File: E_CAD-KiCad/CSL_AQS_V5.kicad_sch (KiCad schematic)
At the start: 10 parts, among them J2 Grove STEMMA, J3 Grove STEMMA

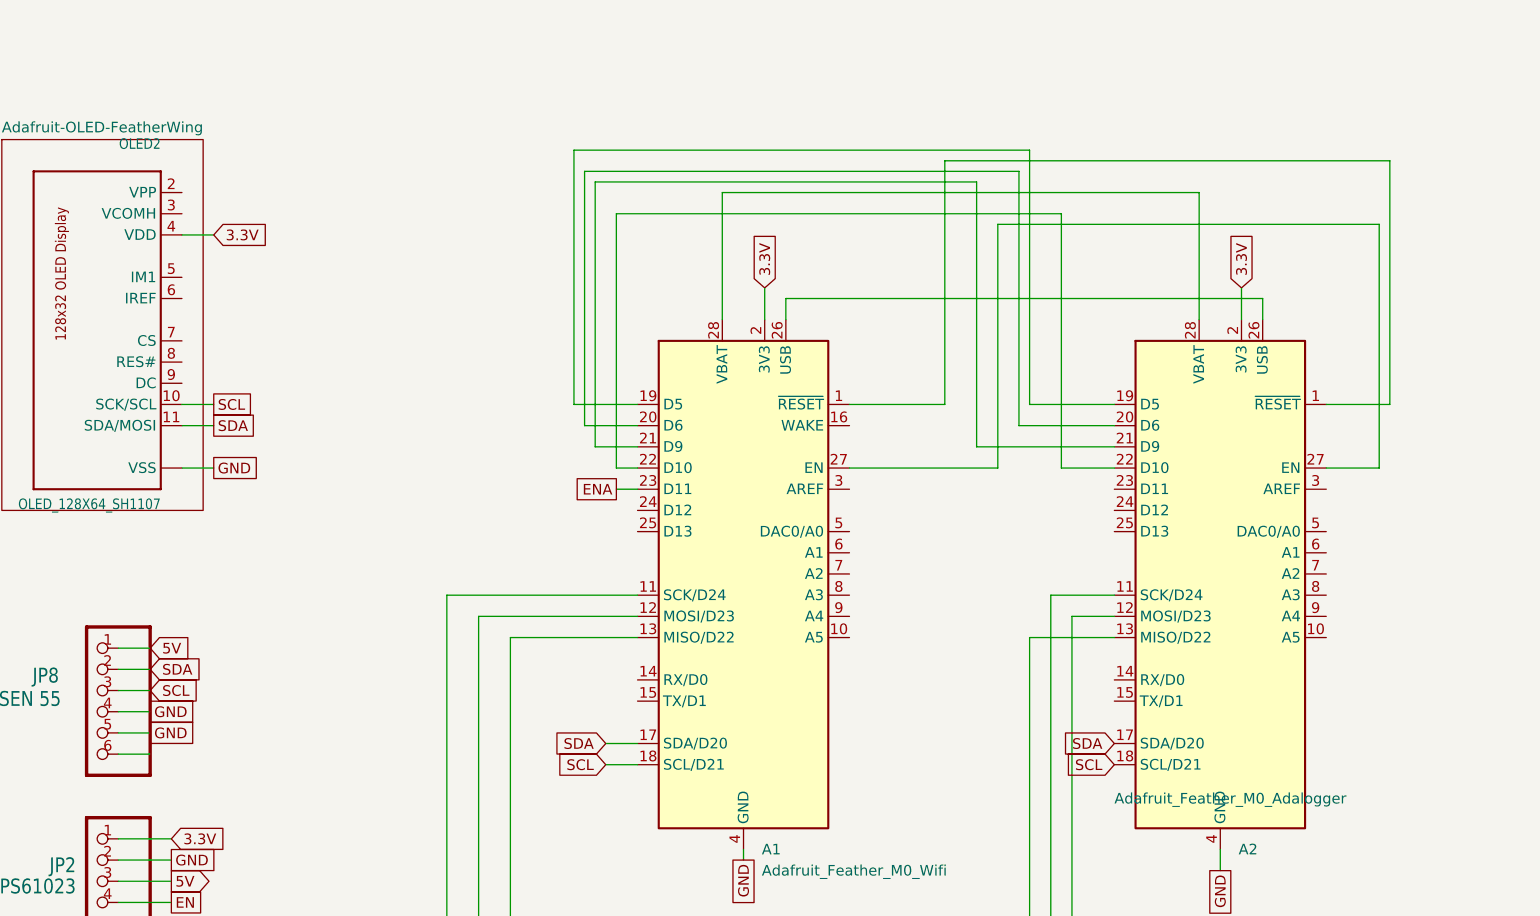
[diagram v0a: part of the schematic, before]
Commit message: Reorganized E-CAD to updated version (5)
Updated to most recent version, version 5
Made updates to the schematic and PCB board in relation to SEN55
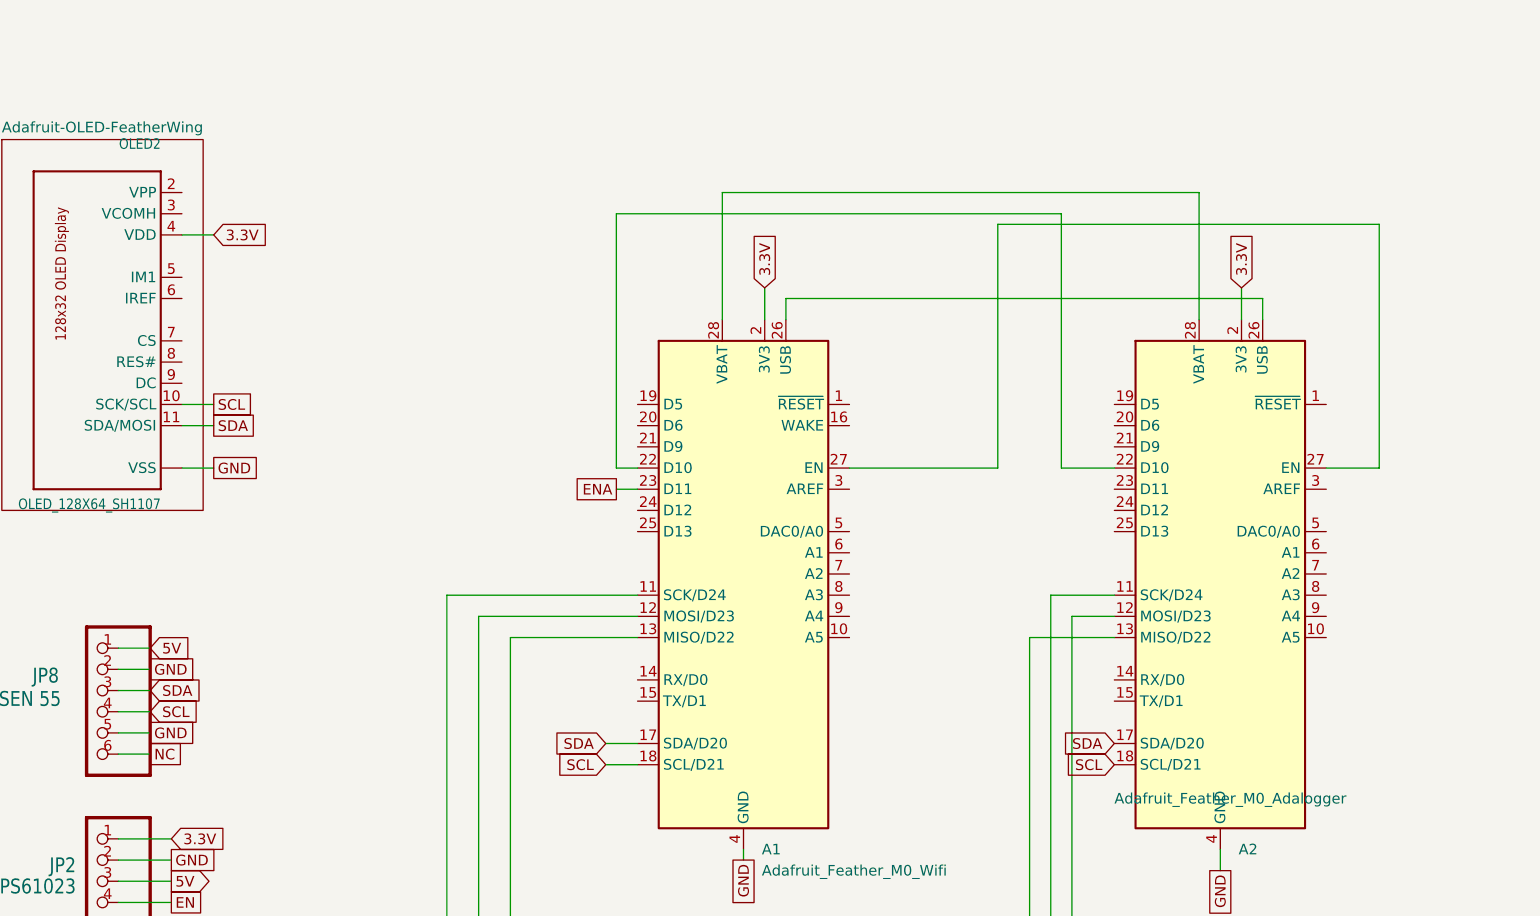
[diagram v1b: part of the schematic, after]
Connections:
- net GND: now also JP8.2; no longer JP8.4
- net NC: now also JP8.6
- net SCL: now also JP8.4; no longer JP8.3
- net SDA: now also JP8.3; no longer JP8.2
- net at A1.1 (~{RESET}): no longer A2.1 (~{RESET})
- net at A1.19 (D5): no longer A2.19 (D5)
- net at A1.20 (D6): no longer A2.20 (D6)
- net at A1.21 (D9): no longer A2.21 (D9)
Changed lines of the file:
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@@
 	(wire
 		(pts
-			(xy 139.7 69.85) (xy 149.86 69.85)
-		)
-		(stroke
-			(width 0)
-			(type default)
-		)
-	)
-	(wire
-		(pts
-			(xy 133.35 43.18) (xy 133.35 74.93)
+			(xy 30.48 104.14) (xy 34.29 104.14)
 		)
 		(stroke
@@
 	(wire
 		(pts
-			(xy 182.88 40.64) (xy 182.88 69.85)
-		)
-		(stroke
-			(width 0)
-			(type default)
-		)
-	)
-	(wire
-		(pts
 			(xy 91.44 175.26) (xy 93.98 175.26)
 		)
@@
 	(wire
 		(pts
-			(xy 129.54 40.64) (xy 182.88 40.64)
-		)
-		(stroke
-			(width 0)
-			(type default)
-		)
-	)
-	(wire
-		(pts
 			(xy 30.48 148.59) (xy 35.56 148.59)
 		)
@@
 	(wire
 		(pts
-			(xy 87.63 43.18) (xy 133.35 43.18)
-		)
-		(stroke
-			(width 0)
-			(type default)
-		)
-	)
-	(wire
-		(pts
-			(xy 129.54 69.85) (xy 129.54 40.64)
-		)
-		(stroke
-			(width 0)
-			(type default)
-		)
-	)
-	(wire
-		(pts
 			(xy 30.48 124.46) (xy 36.83 124.46)
 		)
@@
 	(wire
 		(pts
-			(xy 138.43 72.39) (xy 149.86 72.39)
-		)
-		(stroke
-			(width 0)
-			(type default)
-		)
-	)
-	(wire
-		(pts
 			(xy 30.48 151.13) (xy 35.56 151.13)
 		)
@@
 	(wire
 		(pts
-			(xy 85.09 69.85) (xy 85.09 39.37)
-		)
-		(stroke
-			(width 0)
-			(type default)
-		)
-	)
-	(wire
-		(pts
 			(xy 160.02 59.69) (xy 160.02 44.45)
 		)
@@
 	(wire
 		(pts
+			(xy 30.48 101.6) (xy 34.29 101.6)
+		)
+		(stroke
+			(width 0)
+			(type default)
+		)
+	)
+	(wire
+		(pts
 			(xy 30.48 153.67) (xy 35.56 153.67)
 		)
@@
 	(wire
 		(pts
+			(xy 30.48 106.68) (xy 34.29 106.68)
+		)
+		(stroke
+			(width 0)
+			(type default)
+		)
+	)
+	(wire
+		(pts
 			(xy 139.7 97.79) (xy 149.86 97.79)
 		)
@@
 	(wire
 		(pts
-			(xy 118.11 69.85) (xy 129.54 69.85)
-		)
-		(stroke
-			(width 0)
-			(type default)
-		)
-	)
-	(wire
-		(pts
-			(xy 182.88 69.85) (xy 175.26 69.85)
-		)
-		(stroke
-			(width 0)
-			(type default)
-		)
-	)
-	(wire
-		(pts
 			(xy 88.9 113.03) (xy 92.71 113.03)
 		)
@@
 	(wire
 		(pts
-			(xy 87.63 74.93) (xy 87.63 43.18)
-		)
-		(stroke
-			(width 0)
-			(type default)
-		)
-	)
-	(wire
-		(pts
 			(xy 165.1 55.88) (xy 165.1 59.69)
 		)
@@
 	(wire
 		(pts
-			(xy 139.7 39.37) (xy 139.7 69.85)
-		)
-		(stroke
-			(width 0)
-			(type default)
-		)
-	)
-	(wire
-		(pts
 			(xy 91.44 177.8) (xy 93.98 177.8)
 		)
@@
 	(wire
 		(pts
-			(xy 30.48 101.6) (xy 34.29 101.6)
-		)
-		(stroke
-			(width 0)
-			(type default)
-		)
-	)
-	(wire
-		(pts
 			(xy 92.71 92.71) (xy 69.85 92.71)
 		)
@@
 	(wire
 		(pts
-			(xy 138.43 41.91) (xy 138.43 72.39)
-		)
-		(stroke
-			(width 0)
-			(type default)
-		)
-	)
-	(wire
-		(pts
 			(xy 135.89 48.26) (xy 181.61 48.26)
 		)
@@
 	(wire
 		(pts
-			(xy 86.36 72.39) (xy 86.36 41.91)
-		)
-		(stroke
-			(width 0)
-			(type default)
-		)
-	)
-	(wire
-		(pts
-			(xy 92.71 74.93) (xy 87.63 74.93)
-		)
-		(stroke
-			(width 0)
-			(type default)
-		)
-	)
-	(wire
-		(pts
 			(xy 30.48 121.92) (xy 36.83 121.92)
 		)
@@
 	(wire
 		(pts
-			(xy 133.35 74.93) (xy 149.86 74.93)
-		)
-		(stroke
-			(width 0)
-			(type default)
-		)
-	)
-	(wire
-		(pts
 			(xy 73.66 137.16) (xy 144.78 137.16)
 		)
@@
 	(wire
 		(pts
-			(xy 85.09 39.37) (xy 139.7 39.37)
-		)
-		(stroke
-			(width 0)
-			(type default)
-		)
-	)
-	(wire
-		(pts
 			(xy 167.64 59.69) (xy 167.64 57.15)
 		)
@@
 	(wire
 		(pts
-			(xy 92.71 72.39) (xy 86.36 72.39)
-		)
-		(stroke
-			(width 0)
-			(type default)
-		)
-	)
-	(wire
-		(pts
 			(xy 38.1 77.47) (xy 41.91 77.47)
 		)
@@
 	(wire
 		(pts
-			(xy 30.48 104.14) (xy 34.29 104.14)
-		)
-		(stroke
-			(width 0)
-			(type default)
-		)
-	)
-	(wire
-		(pts
 			(xy 60.96 165.1) (xy 64.77 165.1)
 		)
@@
 	(wire
 		(pts
-			(xy 30.48 106.68) (xy 34.29 106.68)
-		)
-		(stroke
-			(width 0)
-			(type default)
-		)
-	)
-	(wire
-		(pts
 			(xy 77.47 134.62) (xy 139.7 134.62)
 		)
@@
 	(wire
 		(pts
-			(xy 92.71 69.85) (xy 85.09 69.85)
-		)
-		(stroke
-			(width 0)
-			(type default)
-		)
-	)
-	(wire
-		(pts
 			(xy 92.71 95.25) (xy 73.66 95.25)
 		)
@@
 		(pts
 			(xy 90.17 77.47) (xy 90.17 46.99)
-		)
-		(stroke
-			(width 0)
-			(type default)
-		)
-	)
-	(wire
-		(pts
-			(xy 86.36 41.91) (xy 138.43 41.91)
 		)
 		(stroke
@@
 	(global_label "GND"
 		(shape passive)
-		(at 34.29 106.68 0)
-		(fields_autoplaced yes)
-		(effects
-			(font
-				(size 1.27 1.27)
-			)
-			(justify left)
-		)
-		(property "Intersheetrefs" "${INTERSHEET_REFS}"
-			(at 40.0344 106.68 0)
+		(at 34.29 101.6 0)
+		(fields_autoplaced yes)
+		(effects
+			(font
+				(size 1.27 1.27)
+			)
+			(justify left)
+		)
+		(property "Intersheetrefs" "${INTERSHEET_REFS}"
+			(at 40.0344 101.6 0)
 			(effects
 				(font
@@
 	(global_label "SDA"
 		(shape input)
-		(at 34.29 101.6 0)
-		(fields_autoplaced yes)
-		(effects
-			(font
-				(size 1.27 1.27)
-			)
-			(justify left)
-		)
-		(property "Intersheetrefs" "${INTERSHEET_REFS}"
-			(at 40.8433 101.6 0)
+		(at 34.29 104.14 0)
+		(fields_autoplaced yes)
+		(effects
+			(font
+				(size 1.27 1.27)
+			)
+			(justify left)
+		)
+		(property "Intersheetrefs" "${INTERSHEET_REFS}"
+			(at 40.8433 104.14 0)
 			(effects
 				(font
@@
 	(global_label "SCL"
 		(shape input)
-		(at 34.29 104.14 0)
-		(fields_autoplaced yes)
-		(effects
-			(font
-				(size 1.27 1.27)
-			)
-			(justify left)
-		)
-		(property "Intersheetrefs" "${INTERSHEET_REFS}"
-			(at 40.7828 104.14 0)
+		(at 34.29 106.68 0)
+		(fields_autoplaced yes)
+		(effects
+			(font
+				(size 1.27 1.27)
+			)
+			(justify left)
+		)
+		(property "Intersheetrefs" "${INTERSHEET_REFS}"
+			(at 40.7828 106.68 0)
 			(effects
 				(font
@@
 		(property "Intersheetrefs" "${INTERSHEET_REFS}"
 			(at 40.0344 148.59 0)
+			(effects
+				(font
+					(size 1.27 1.27)
+				)
+				(justify left)
+				(hide yes)
+			)
+		)
+	)
+	(global_label "NC"
+		(shape passive)
+		(at 34.29 111.76 0)
+		(fields_autoplaced yes)
+		(effects
+			(font
+				(size 1.27 1.27)
+			)
+			(justify left)
+		)
+		(property "Intersheetrefs" "${INTERSHEET_REFS}"
+			(at 38.7644 111.76 0)
 			(effects
 				(font
@@
 		)
 		(instances
-			(project "CSL_AQS_V1"
+			(project "CSL_AQS_V5"
 				(path "/0298e1a2-41ac-46e9-9543-4e7b3ae3dfa6"
 					(page "4")
@@
 		)
 		(instances
-			(project "CSL_AQS_V1"
+			(project "CSL_AQS_V5"
 				(path "/0298e1a2-41ac-46e9-9543-4e7b3ae3dfa6"
 					(page "3")
@@
 		)
 		(instances
-			(project "CSL_AQS_V1"
+			(project "CSL_AQS_V5"
 				(path "/0298e1a2-41ac-46e9-9543-4e7b3ae3dfa6"
 					(page "2")

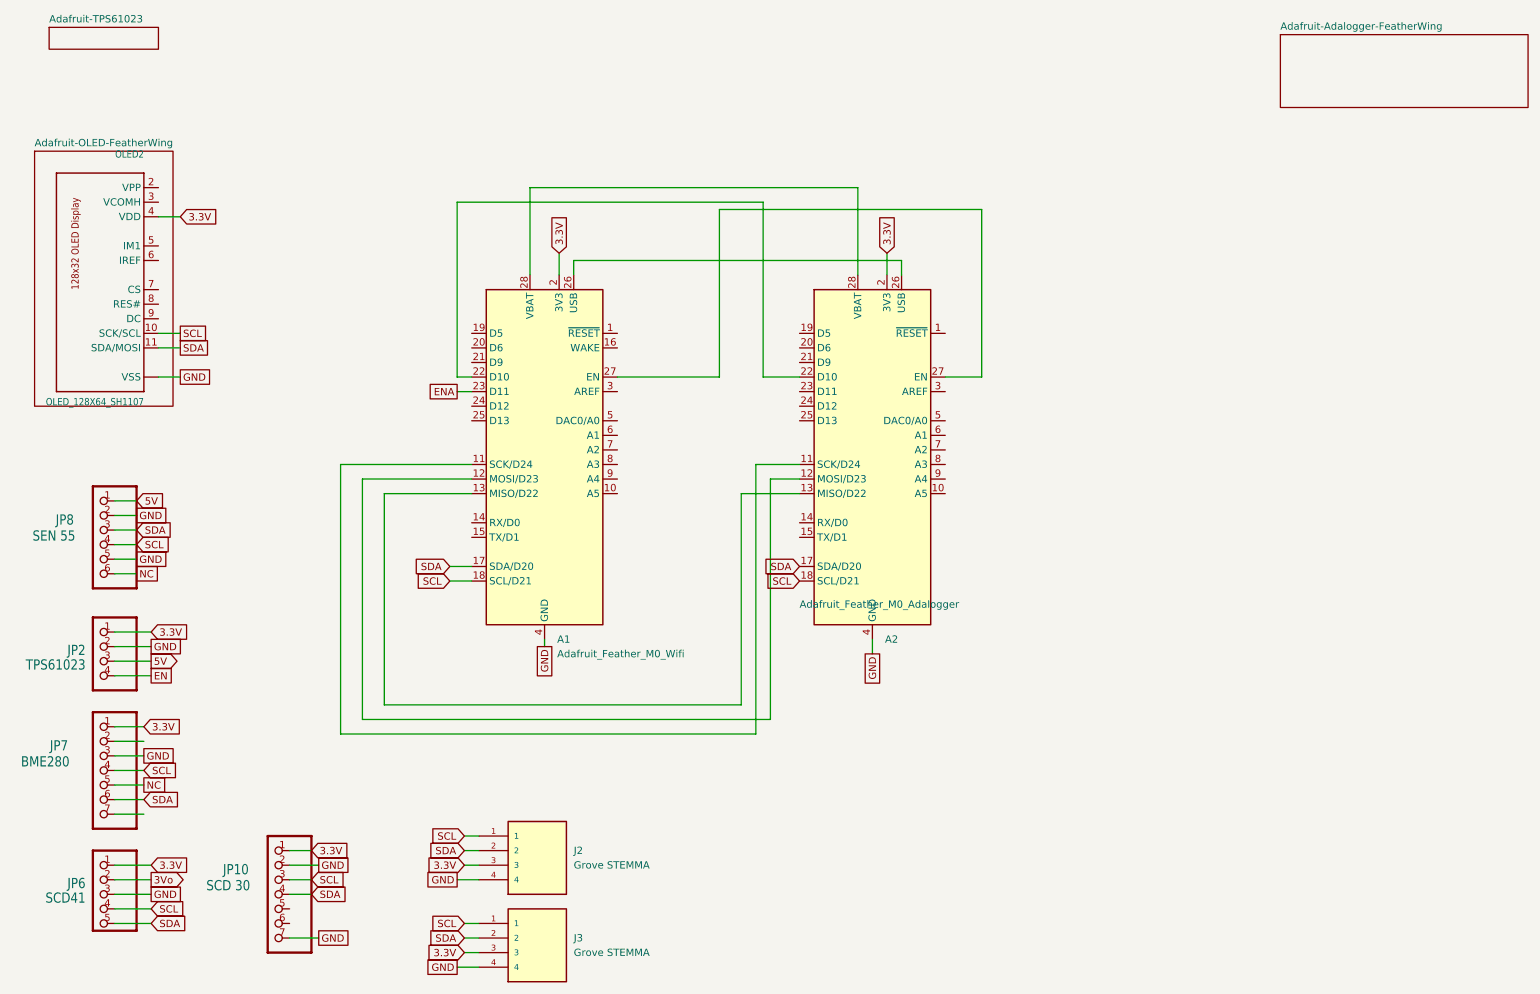
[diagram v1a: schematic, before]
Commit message: Updated E-CAD File
Revisited a missed connection in the E-CAD files. Placement of the OLED when resetting should now function regardless of the board it is stacked on.
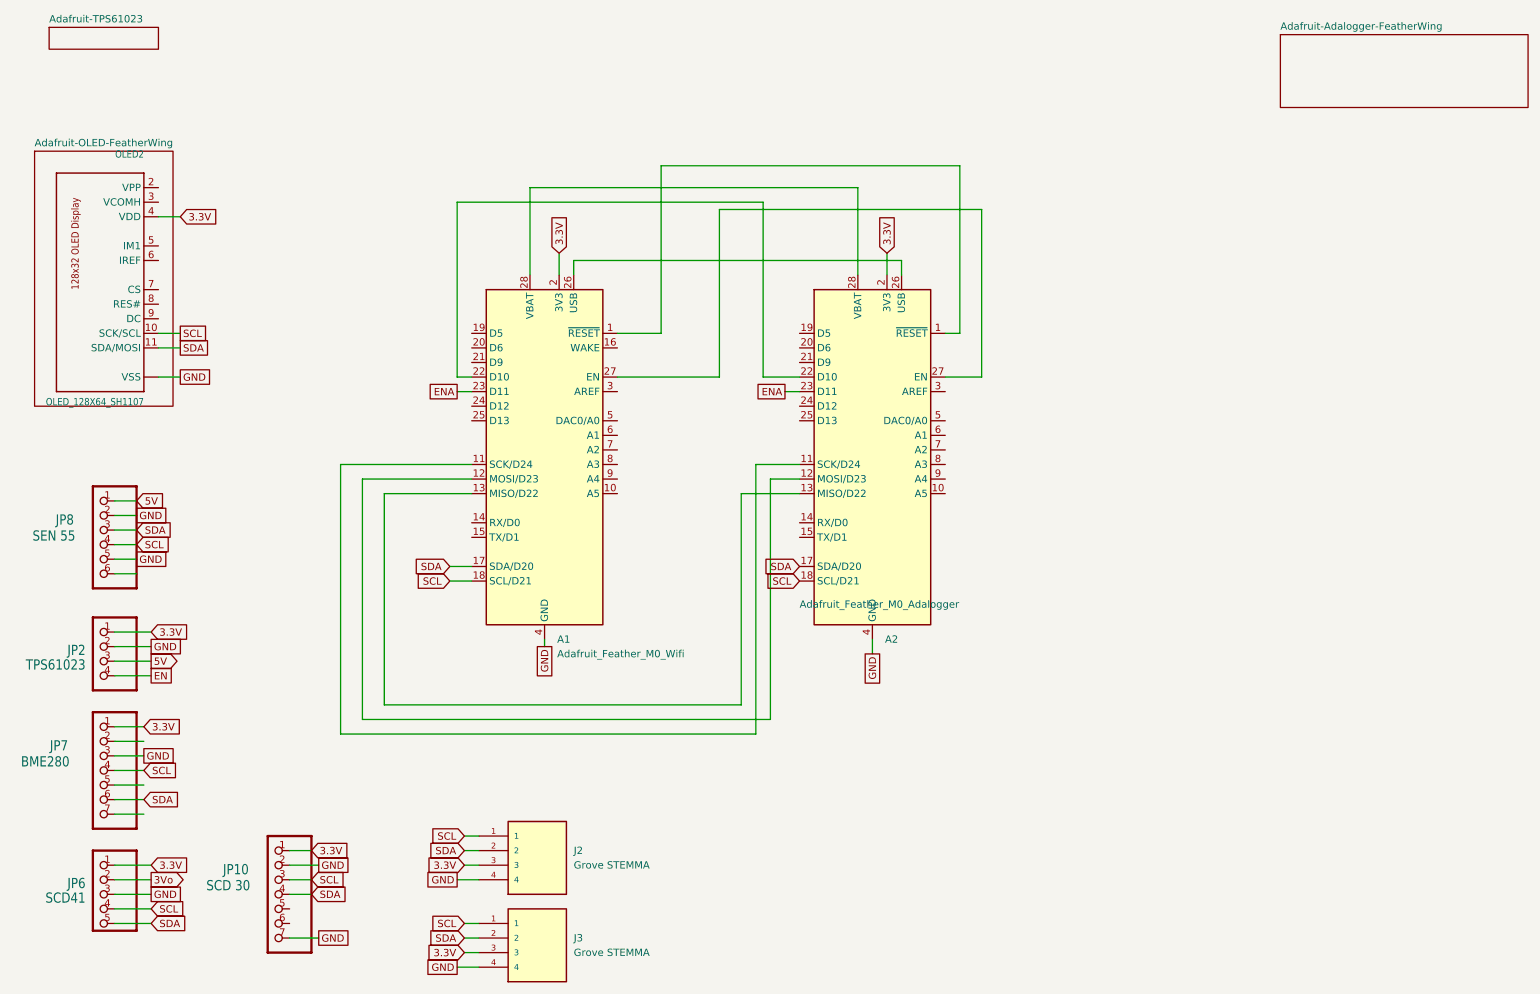
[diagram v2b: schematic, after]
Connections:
- net ENA: now also A2.23 (D11)
- net at A1.1 (~{RESET}): now also A2.1 (~{RESET})
- net NC: no longer names the net of JP7.5
- net NC: no longer JP8.6
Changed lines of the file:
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@@
+	(wire
+		(pts
+			(xy 147.32 80.01) (xy 149.86 80.01)
+		)
+		(stroke
+			(width 0)
+			(type default)
+		)
+	)
 	(wire
 		(pts
@@
 	(wire
 		(pts
+			(xy 177.8 69.85) (xy 175.26 69.85)
+		)
+		(stroke
+			(width 0)
+			(type default)
+		)
+	)
+	(wire
+		(pts
 			(xy 30.48 151.13) (xy 35.56 151.13)
 		)
@@
 	(wire
 		(pts
+			(xy 125.73 40.64) (xy 177.8 40.64)
+		)
+		(stroke
+			(width 0)
+			(type default)
+		)
+	)
+	(wire
+		(pts
 			(xy 30.48 101.6) (xy 34.29 101.6)
 		)
@@
 	(wire
 		(pts
+			(xy 125.73 69.85) (xy 125.73 40.64)
+		)
+		(stroke
+			(width 0)
+			(type default)
+		)
+	)
+	(wire
+		(pts
 			(xy 38.1 69.85) (xy 41.91 69.85)
 		)
@@
 	(wire
 		(pts
+			(xy 177.8 40.64) (xy 177.8 69.85)
+		)
+		(stroke
+			(width 0)
+			(type default)
+		)
+	)
+	(wire
+		(pts
 			(xy 60.96 165.1) (xy 64.77 165.1)
 		)
@@
 		(pts
 			(xy 90.17 77.47) (xy 90.17 46.99)
+		)
+		(stroke
+			(width 0)
+			(type default)
+		)
+	)
+	(wire
+		(pts
+			(xy 118.11 69.85) (xy 125.73 69.85)
 		)
 		(stroke
@@
 		)
 	)
-	(global_label "NC"
+	(global_label "ENA"
 		(shape passive)
-		(at 35.56 148.59 0)
-		(fields_autoplaced yes)
-		(effects
-			(font
-				(size 1.27 1.27)
-			)
-			(justify left)
-		)
-		(property "Intersheetrefs" "${INTERSHEET_REFS}"
-			(at 40.0344 148.59 0)
-			(effects
-				(font
-					(size 1.27 1.27)
-				)
-				(justify left)
-				(hide yes)
-			)
-		)
-	)
-	(global_label "NC"
-		(shape passive)
-		(at 34.29 111.76 0)
-		(fields_autoplaced yes)
-		(effects
-			(font
-				(size 1.27 1.27)
-			)
-			(justify left)
-		)
-		(property "Intersheetrefs" "${INTERSHEET_REFS}"
-			(at 38.7644 111.76 0)
-			(effects
-				(font
-					(size 1.27 1.27)
-				)
-				(justify left)
-				(hide yes)
-			)
+		(at 147.32 80.01 180)
+		(fields_autoplaced yes)
+		(effects
+			(font
+				(size 1.27 1.27)
+			)
+			(justify right)
+		)
+		(property "Intersheetrefs" "${INTERSHEET_REFS}"
+			(at 141.878 80.01 0)
+			(effects
+				(font
+					(size 1.27 1.27)
+				)
+				(justify right)
+				(hide yes)
+			)
